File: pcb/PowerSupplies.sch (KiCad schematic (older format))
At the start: 21 parts, among them P65 GND/5v, Q12 KSH127TF, U13 TL431BQDBZR, U2 LM2940T-5.0, U3 LM2940T-5.0

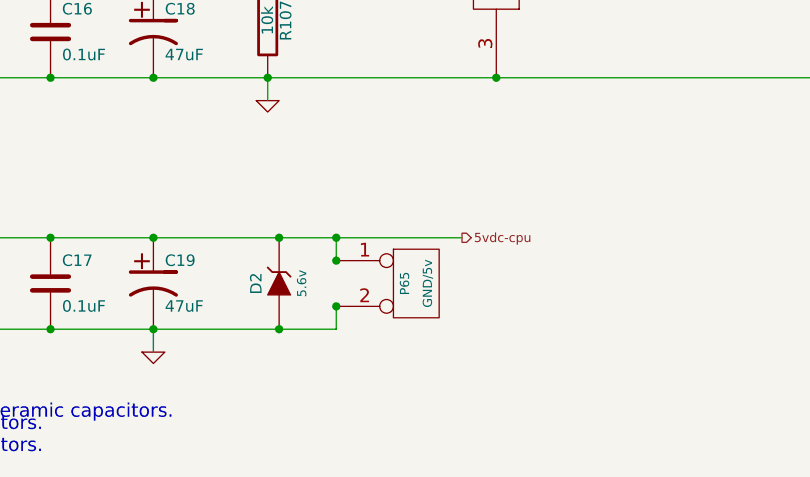
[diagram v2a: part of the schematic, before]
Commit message: Eliminated Pxx designations on the wire connection points and replaced them with the PCB silkscreen designations.
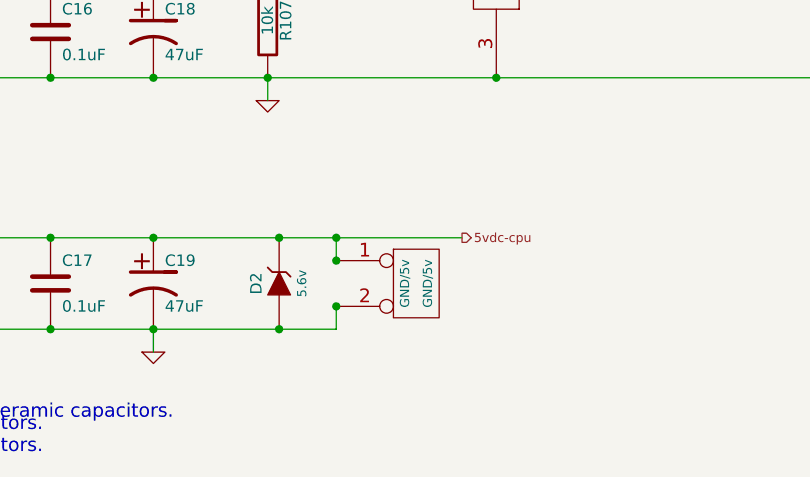
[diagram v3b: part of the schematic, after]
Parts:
- renumbered P65 to GND/5v
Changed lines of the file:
@@
 Sheet 7 7
 Title "Jaguar PCB for FreeEMS"
-Date "17 nov 2013"
+Date "3 dec 2013"
 Rev "0.6-alpha"
 Comp "Git: 73f4fbd6d6"
@@
 Connection ~ 5350 3350
 $Comp
-L CONN_2 P65
+L CONN_2 GND/5v
 U 1 1 519BE395
 P 5700 3550
-F 0 "P65" V 5650 3550 40  0000 C CNN
+F 0 "GND/5v" V 5650 3550 40  0000 C CNN
 F 1 "GND/5v" V 5750 3550 40  0000 C CNN
 F 2 "" H 5700 3550 60  0001 C CNN

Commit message: Added LEDs and resistors to ignitor outputs.
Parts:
- removed D2: 5.6v, symbol ZENER
- removed GND/5v: GND/5v, symbol CONN_2
- removed Q12: KSH127TF, symbol PNP-BCE
- added JP?: JUMPER, symbol JUMPER
- added Q?: ZXTP25020DGTA, symbol PNP
- U?: renamed from U2; value LM2940T-5.0 -> LM2937EM-5.0
- U?: renamed from U3; value LM2940T-5.0 -> LM2937EM-5.0
- renumbered C12 to C?, C14 to C?, C16 to C?, C18 to C?, C19 to C?, C17 to C?, C15 to C?, C13 to C?, D43 to D?, D44 to D?, MOV1 to MOV?, R107 to R?, R109 to R?, R108 to R?, R106 to R?, U13 to U?
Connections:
- wire segments 23 -> 22
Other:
- note added: "JP9 and JP10 allow you to build the power supply\ncircuits and test them before connecting them\nto the rest of the board."

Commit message: Changed revision to 0.7-alpha and git hash to xxxxxxxxxx to show that this is in progress.
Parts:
- removed JP?: JUMPER, symbol JUMPER
- removed Q?: ZXTP25020DGTA, symbol PNP
- added D2: 5.6v, symbol ZENER
- added GND/5v: GND/5v, symbol CONN_2
- added Q12: KSH127TF, symbol PNP-BCE
- U2, U3: renamed from U?; value LM2937EM-5.0 -> LM2940T-5.0
- gave numbers to parts that had none: 16
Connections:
- wire segments 22 -> 23
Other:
- note removed: "JP9 and JP10 allow you to build the power supply\ncircuits and test them before connecting them\nto the rest of the board."

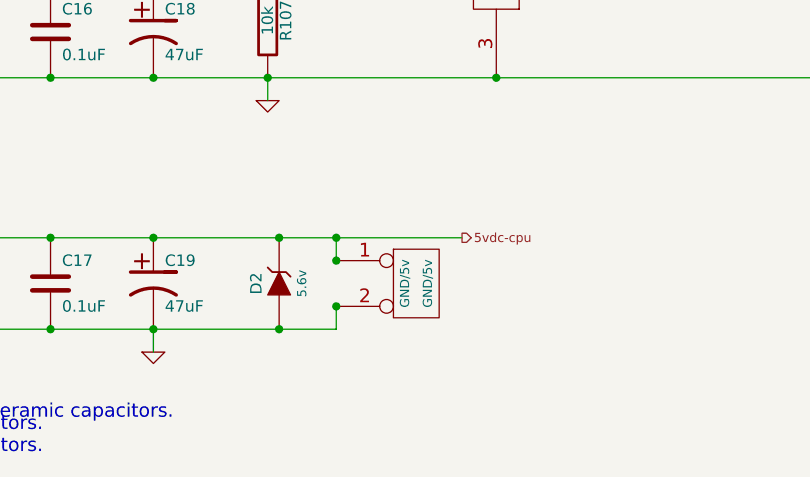
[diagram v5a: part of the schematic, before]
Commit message: Started laying out PCB changes for SO-8 high side driver and new SO-8 low side drivers.
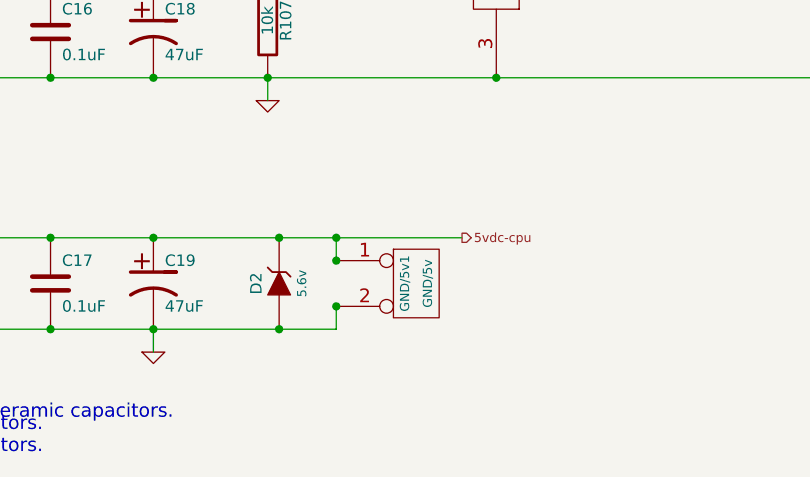
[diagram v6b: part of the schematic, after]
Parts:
- renumbered GND/5v to GND/5v1
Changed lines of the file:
@@
 Sheet 7 7
 Title "Jaguar PCB for FreeEMS"
-Date "5 feb 2014"
+Date "4 mar 2014"
 Rev "0.7-alpha"
 Comp "Git: xxxxxxxxxx"
@@
 Connection ~ 5350 3350
 $Comp
-L CONN_2 GND/5v
+L CONN_2 GND/5v1
 U 1 1 519BE395
 P 5700 3550
-F 0 "GND/5v" V 5650 3550 40  0000 C CNN
+F 0 "GND/5v1" V 5650 3550 40  0000 C CNN
 F 1 "GND/5v" V 5750 3550 40  0000 C CNN
 F 2 "" H 5700 3550 60  0001 C CNN
@@
 12v-switch
 $Comp
-L GND #PWR048
+L GND #PWR53
 U 1 1 4F1C2CDE
 P 4550 3850
-F 0 "#PWR048" H 4550 3850 30  0001 C CNN
+F 0 "#PWR53" H 4550 3850 30  0001 C CNN
 F 1 "GND" H 4550 3780 30  0001 C CNN
 F 2 "" H 4550 3850 60  0001 C CNN
@@
 $EndComp
 $Comp
-L GND #PWR049
+L GND #PWR54
 U 1 1 4F1C2CC1
 P 5050 2750
-F 0 "#PWR049" H 5050 2750 30  0001 C CNN
+F 0 "#PWR54" H 5050 2750 30  0001 C CNN
 F 1 "GND" H 5050 2680 30  0001 C CNN
 F 2 "" H 5050 2750 60  0001 C CNN
